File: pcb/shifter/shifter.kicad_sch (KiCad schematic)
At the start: 53 parts, among them J1 USB_B_Micro, J2 AVR-ISP-6, J3 shifter connector, SW1 power select, SW2 test button, U1 FT260S, U2 AT24CS04-SSHM, U3 ATmega48A-A

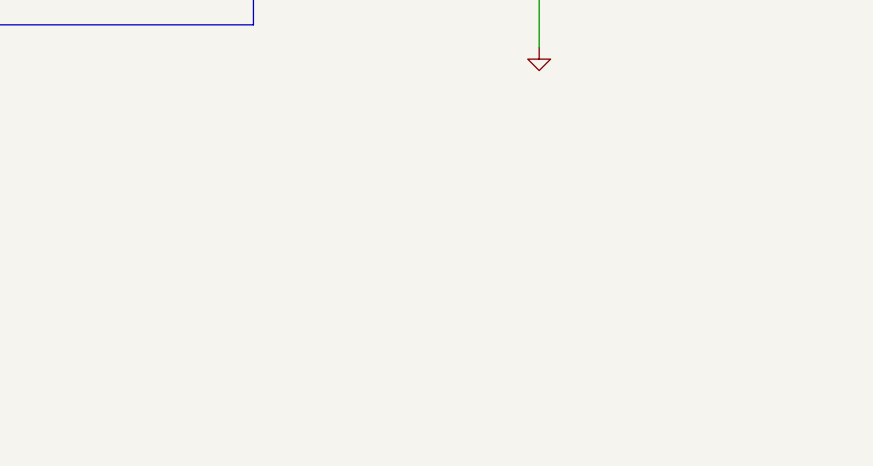
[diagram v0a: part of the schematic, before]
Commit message: added all footprints to schmatic
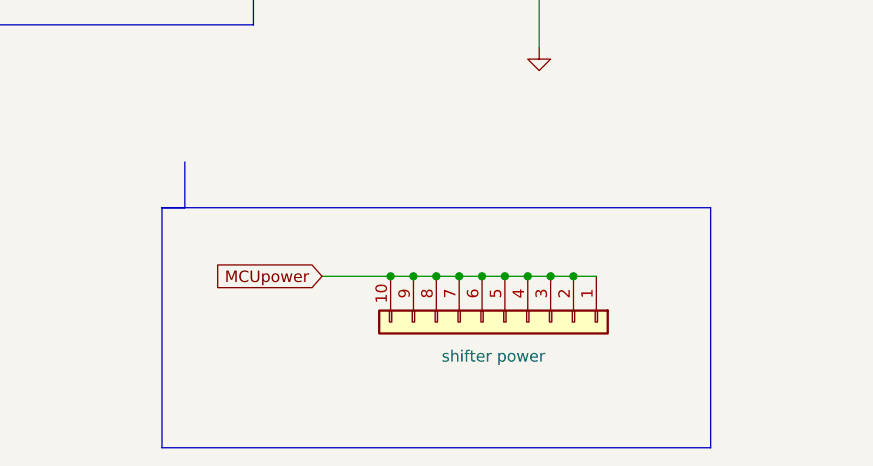
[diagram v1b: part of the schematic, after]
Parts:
- added J4: shifter power, Connector_Wire:SolderWirePad 10 3-3mm, symbol Connector_Generic:Conn_01x10
- C10, C13, C6, C8: footprint Wurth:AGC1206X7R500-475KXE 4.7uF -> Wima:WIMA_XA_WIM
- J2: footprint (none) -> Connector_Harting:Harthing 6 pin
- J3: footprint Wurth:LSF-SMD -> Connector_Wire:SolderWirePad 10 3-3mm
- SW1: footprint (none) -> powerSelector:SW_JS202011SCQN
- SW2: footprint (none) -> Wurth:TactileButton
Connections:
- net MCUpower: now also J4.1 (Pin_1), J4.10 (Pin_10), J4.2 (Pin_2), J4.3 (Pin_3), J4.4 (Pin_4), J4.5 (Pin_5), J4.6 (Pin_6), J4.7 (Pin_7), J4.8 (Pin_8), J4.9 (Pin_9)
